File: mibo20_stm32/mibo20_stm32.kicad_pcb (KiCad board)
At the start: 2 copper layers, 33 x 17.8 mm, 24 parts, among them J1 Conn_01x02, J2 Conn_01x13, J3 Conn_01x13, J4 USB_B_Micro, J5 Conn_01x04, SW1 Reset, U1 STM32x0xxFxPx, U2 AMS1117-3.3, Y1 8MHz

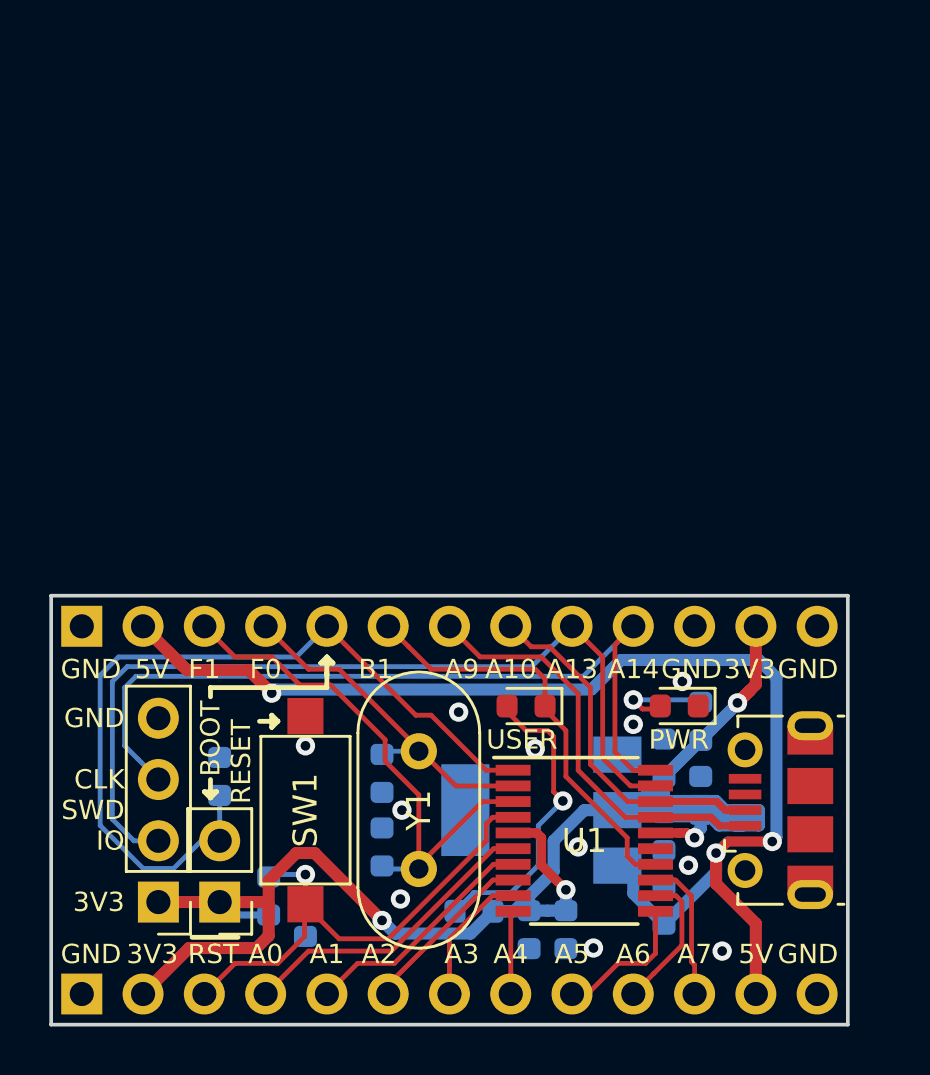
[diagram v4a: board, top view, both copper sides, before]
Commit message: SWD connector rotated
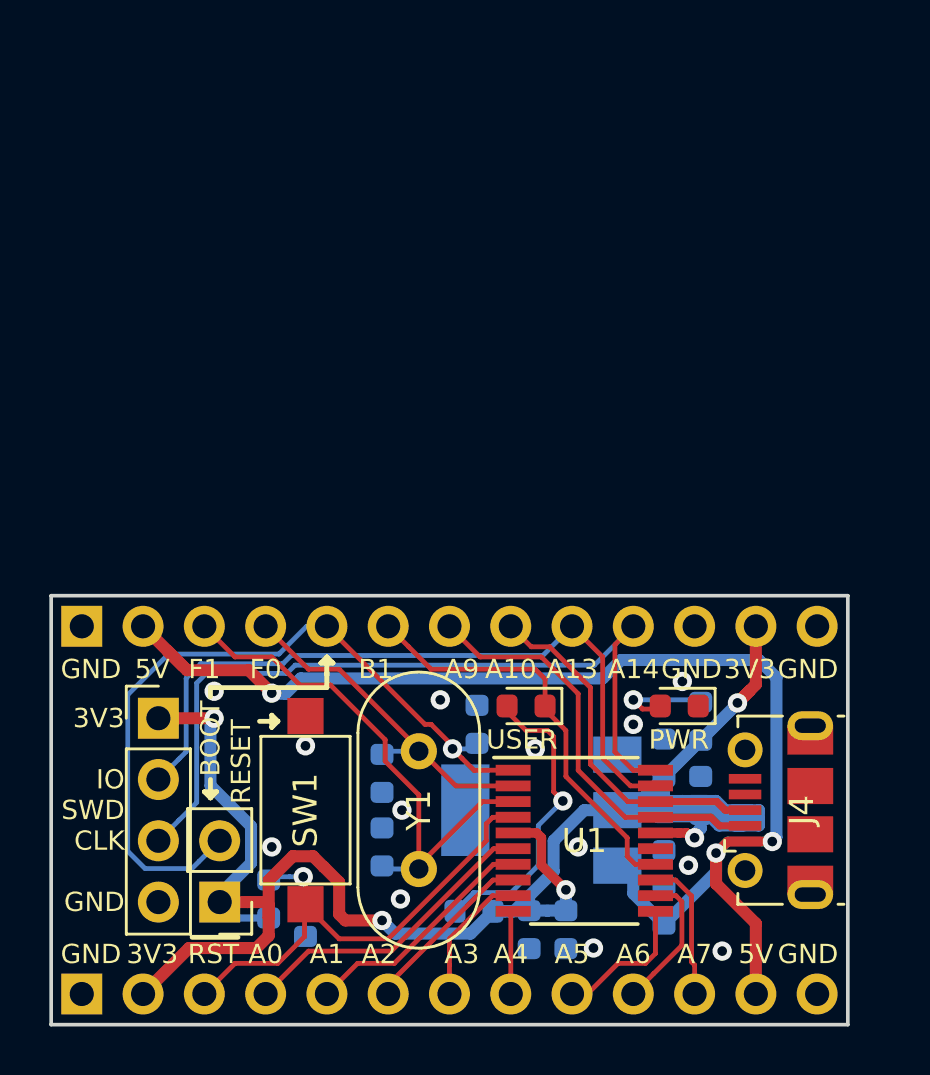
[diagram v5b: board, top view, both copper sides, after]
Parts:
- moved R1 10.9 mm to (153.5, 93.0)
- moved J5 7.62 mm to (140.3, 92.7), turned to 0 degrees
- moved R2 0.13 mm to (144.9, 100.2)
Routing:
- net +3V3: track 75.0 -> 84.3 mm, vias 4 -> 5
- net /PA13: track 36.6 -> 30.2 mm
- net /BOOT0: track 34.7 -> 32.6 mm, vias 0 -> 1
- net GND: vias 11 -> 13

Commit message: Q1 and SW1 swapped
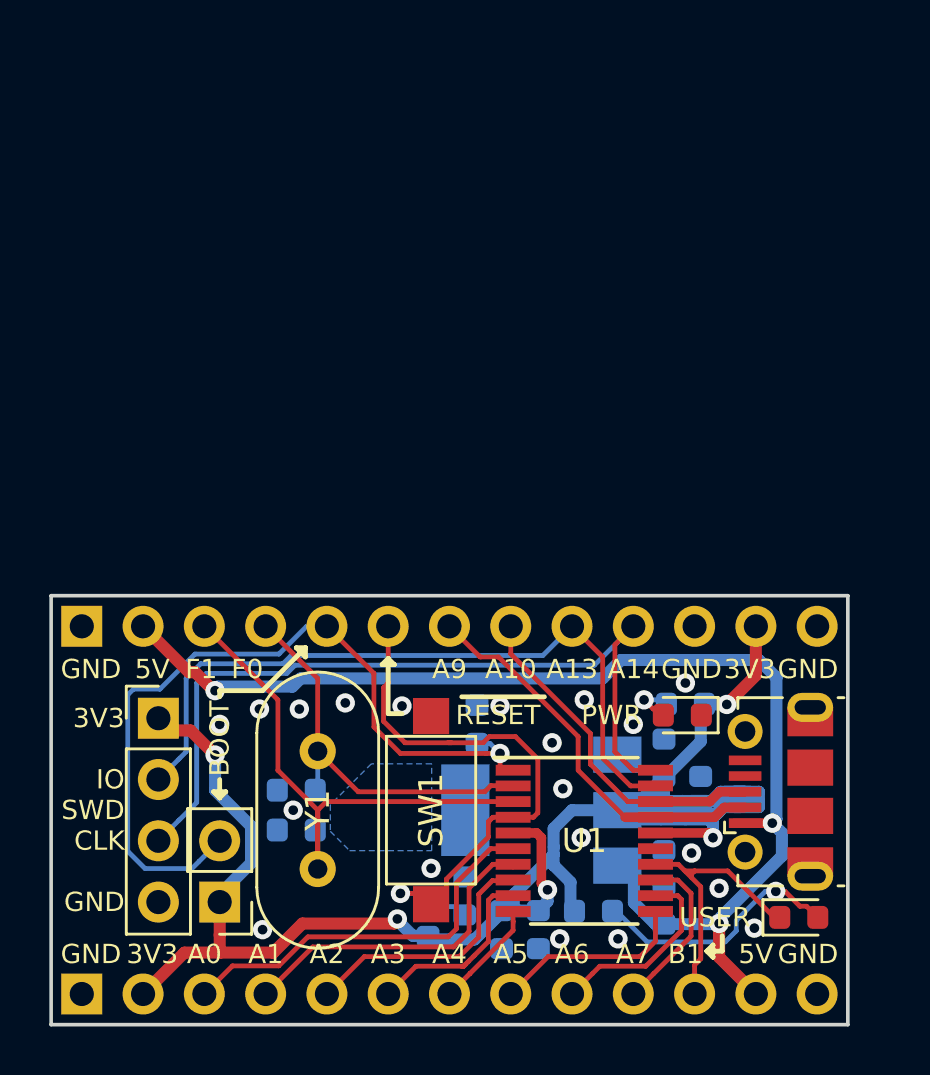
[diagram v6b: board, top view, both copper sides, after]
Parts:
- moved D1 14.3 mm to (166.9, 101.0), turned to 0 degrees
- moved C3 6.66 mm to (153.0, 100.1), turned to 90 degrees
- moved R2 6.65 mm to (151.5, 101.0)
- moved SW1 5.21 mm to (151.6, 96.5)
- moved R3 4.95 mm to (158.4, 100.7), turned to 180 degrees
- moved Y1 4.19 mm to (146.9, 94.1)
- moved C1 3.62 mm to (146.1, 95.7), turned to 180 degrees
- moved C2 3.62 mm to (146.1, 97.3), turned to 180 degrees
- moved C6 1.14 mm to (156.1, 101.5)
- moved C7 1.14 mm to (154.6, 101.5)
- moved R4 0.95 mm to (162.2, 92.1), turned to 0 degrees
- moved J4 0.76 mm to (166.1, 95.8)
- moved D2 0.40 mm to (162.1, 92.6)
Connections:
- J2 pad 10: /PA6 -> /PA7
- J2 pad 11: /PA7 -> /LED1
- J2 pad 3: /RESET -> /PA0
- J2 pad 4: /PA0 -> /PA1
- J2 pad 5: /PA1 -> /PA2
- J2 pad 6: /PA2 -> /PA3
- J2 pad 7: /PA3 -> /PA4
- J2 pad 8: /PA4 -> /PA5
- J2 pad 9: /PA5 -> /PA6
- J3 pad 6: /LED1 -> /RESET
- J4 pad 4: (no net) -> Net-(J4-Pad4)
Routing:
- net /LED1: track 17.5 -> 11.8 mm
- net /5V: track 54.3 -> 50.3 mm
- net /PA1: track 9.94 -> 13.7 mm
- net /PA0: track 12.8 -> 16.5 mm
- net +3V3: track 84.3 -> 87.7 mm
- net /PA2: track 7.36 -> 10.7 mm
- net /PA6: track 5.86 -> 8.69 mm
- net /PA3: track 5.67 -> 7.99 mm
- net /RESET: track 21.9 -> 24.2 mm
- net /PA5: track 5.90 -> 8.14 mm
- net Net-(D2-Pad2): track 4.11 -> 1.96 mm
- net /OSC_OUT: track 22.4 -> 24.4 mm
- net /OSC_IN: track 14.7 -> 16.7 mm
- net /BOOT0: track 32.6 -> 34.6 mm
- net Net-(D1-Pad2): track 12.6 -> 10.7 mm
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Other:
- board text removed: "RST"

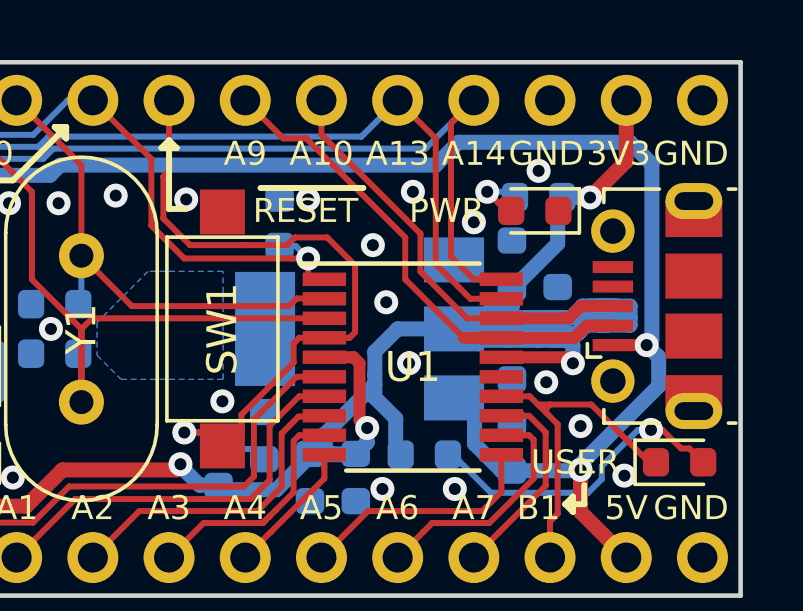
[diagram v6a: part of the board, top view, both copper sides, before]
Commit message: Jumper for USB added
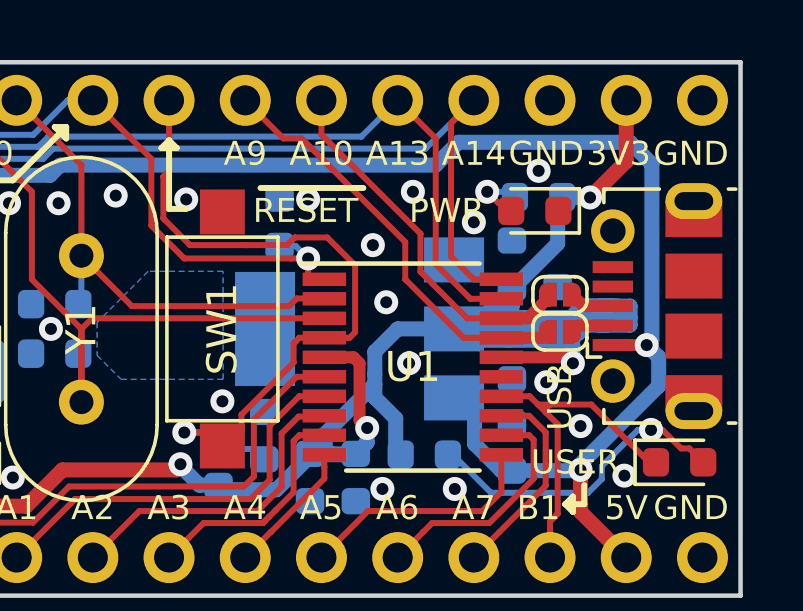
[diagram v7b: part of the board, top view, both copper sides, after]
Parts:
- added JP1: SolderJumper_2_Open, mibo20_stm32:SolderJumper-2_P0.8mm_Open_RoundedPad0.6x0.8mm, F.Cu at (162.9, 95.4)
- added JP2: SolderJumper_2_Open, mibo20_stm32:SolderJumper-2_P0.8mm_Open_RoundedPad0.6x0.8mm, F.Cu at (162.9, 96.6)
- U1: value STM32x0xxFxPx -> STM32F070F6Px
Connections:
- J4 pad 2: /PA11 -> Net-(J4-Pad2)
- J4 pad 3: /PA10 -> Net-(J4-Pad3)
- J4 pad 4: Net-(J4-Pad4) -> (no net)
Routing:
- net /PA11: track 16.5 -> 14.2 mm
- net /PA10: track 14.3 -> 12.2 mm
- net Net-(J4-Pad3): track 0.00 -> 1.52 mm
- net Net-(J4-Pad2): track 0.00 -> 1.45 mm
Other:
- board text added: "USB"
